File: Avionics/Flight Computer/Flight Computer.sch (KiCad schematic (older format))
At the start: 28 parts, among them U10 Logo, U11 Logo, U6 LP5521YQ

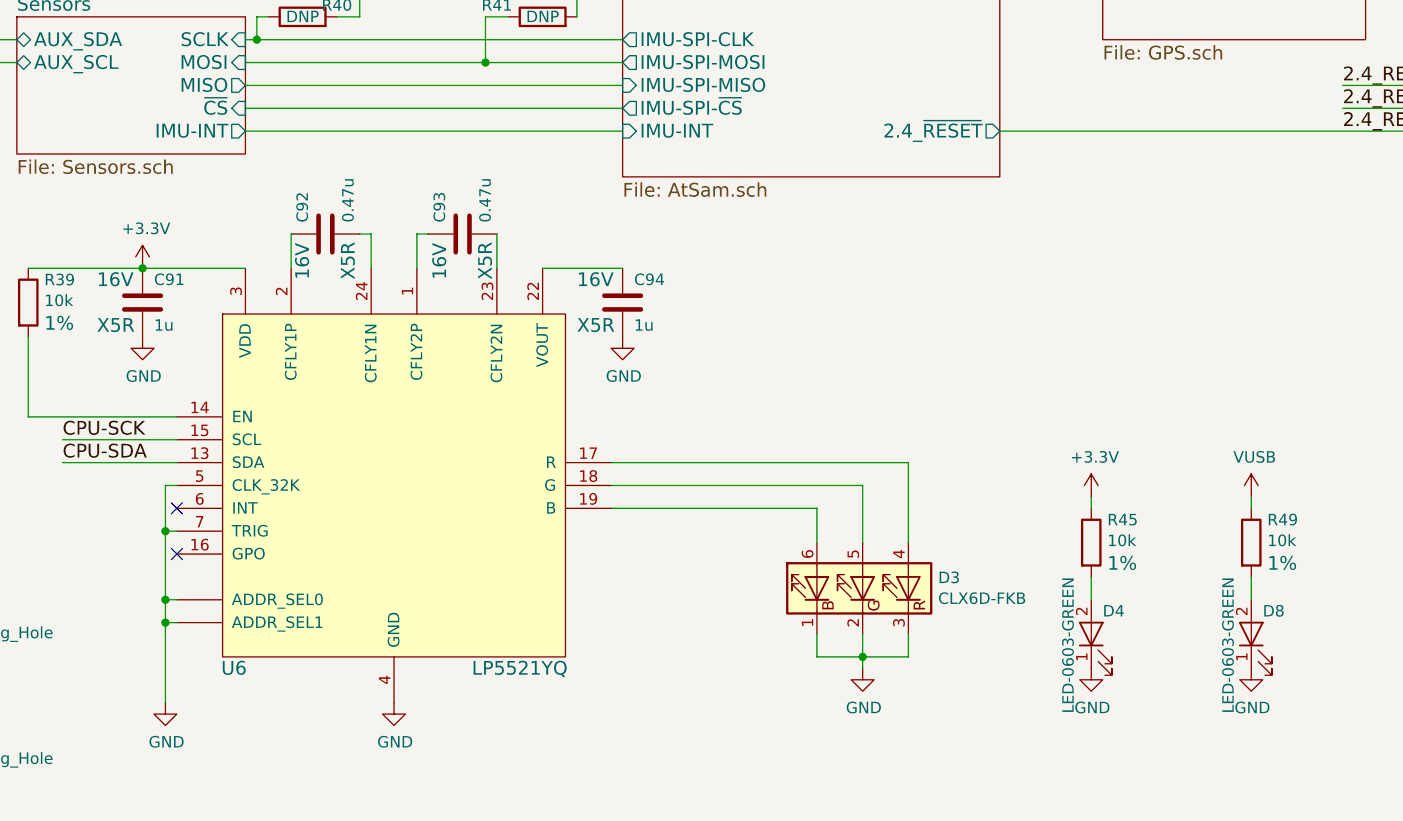
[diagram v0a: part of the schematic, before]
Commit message: Updated more manufacturing part numbers for macrofab compatibility.
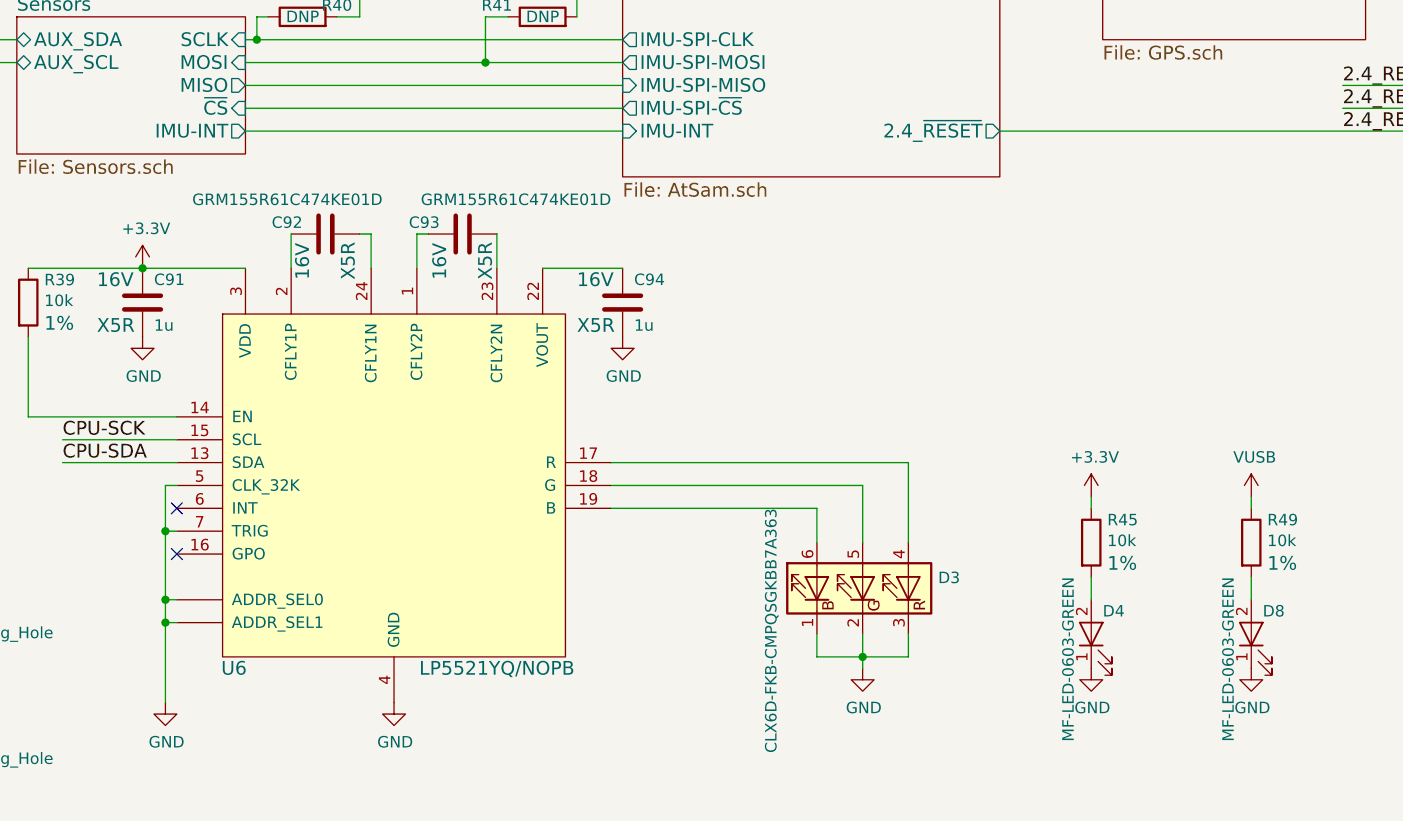
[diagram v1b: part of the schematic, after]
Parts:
- C92, C93: value 0.47u -> GRM155R61C474KE01D
- D3: value CLX6D-FKB -> CLX6D-FKB-CMPQSGKBB7A363
- D4, D8: value LED-0603-GREEN -> MF-LED-0603-GREEN
- U6: value LP5521YQ -> LP5521YQ/NOPB
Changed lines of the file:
@@
 P 5850 7100
 F 0 "D4" V 5950 7050 50  0000 R CNN
-F 1 "LED-0603-GREEN" H 6100 7200 50  0000 R CNN
+F 1 "MF-LED-0603-GREEN" H 6100 7200 50  0000 R CNN
 F 2 "LEDs:LED_0603" H 450 750 50  0001 C CNN
 F 3 "https://s3.amazonaws.com/mfprodpublic/datasheets/S_110_LTST-C190KGKT.pdf" H 450 750 50  0001 C CNN
@@
 P 6550 7100
 F 0 "D8" V 6650 7050 50  0000 R CNN
-F 1 "LED-0603-GREEN" H 6800 7200 50  0000 R CNN
+F 1 "MF-LED-0603-GREEN" H 6800 7200 50  0000 R CNN
 F 2 "LEDs:LED_0603" H 1150 750 50  0001 C CNN
 F 3 "https://s3.amazonaws.com/mfprodpublic/datasheets/S_110_LTST-C190KGKT.pdf" H 1150 750 50  0001 C CNN
@@
 P 4850 6900
 F 0 "D3" V 4896 6570 50  0000 R CNN
-F 1 "CLX6D-FKB" V 4805 6570 50  0000 R CNN
+F 1 "CLX6D-FKB-CMPQSGKBB7A363" H 5200 7300 50  0000 R CNN
 F 2 "LEDs:LED_PLCC6_3.4x3.4mm" H 200 150 50  0001 C CNN
 F 3 "http://www.cree.com/~/media/Files/Cree/LED-Components-and-Modules/HB/Data-Sheets/1278-CLX6D-FKB.pdf" H 200 150 50  0001 C CNN
@@
 U 1 1 58CBE629
 P 2500 5350
-F 0 "C92" H 2550 5450 50  0000 L CNN
-F 1 "0.47u" H 2550 5250 50  0000 L CNN
+F 0 "C92" V 2550 5450 50  0000 L CNN
+F 1 "GRM155R61C474KE01D" V 2650 5100 50  0000 L CNN
 F 2 "Capacitors_SMD:C_0402" H -4012 4050 50  0001 C CNN
 F 3 "" H -4050 4200 50  0001 C CNN
@@
 U 1 1 58CBEC69
 P 3100 5350
-F 0 "C93" H 3150 5450 50  0000 L CNN
-F 1 "0.47u" H 3150 5250 50  0000 L CNN
+F 0 "C93" V 3150 5450 50  0000 L CNN
+F 1 "GRM155R61C474KE01D" V 3250 4700 50  0000 L CNN
 F 2 "Capacitors_SMD:C_0402" H -3412 4050 50  0001 C CNN
 F 3 "" H -3450 4200 50  0001 C CNN
@@
 P 2800 6450
 F 0 "U6" H 2100 5650 60  0000 C CNN
-F 1 "LP5521YQ" H 3350 5650 60  0000 C CNN
+F 1 "LP5521YQ/NOPB" H 3250 5650 60  0000 C CNN
 F 2 "Housings_DFN_QFN:QFN-24-1EP_4x5mm_Pitch0.5mm" H -150 -800 60  0001 C CNN
 F 3 "http://www.digikey.com/product-detail/en/texas-instruments/LP5521YQ-NOPB/LP5521YQ-NOPBCT-ND/1836170" H -200 -950 60  0001 C CNN

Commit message: Finished rerouting and power supply update. Replaced connectors and did initial replacement.
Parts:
- added MK3, MK4: Mounting_Hole, Mounting_Holes:MountingHole_2.5mm, symbol Mounting_Hole
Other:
- moved on the sheet: MK1, MK2
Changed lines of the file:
@@
 LIBS:Power_Management
 LIBS:powerint
+LIBS:onsemi
 LIBS:Flight Computer-cache
 EELAYER 26 0
@@
 L Mounting_Hole MK1
 U 1 1 58BDD655
-P 700 7050
-F 0 "MK1" H 800 7096 50  0000 L CNN
-F 1 "Mounting_Hole" H 800 7005 50  0000 L CNN
-F 2 "Mounting_Holes:MountingHole_2.5mm" H -3500 0   50  0001 C CNN
-F 3 "" H -3500 0   50  0001 C CNN
-	1    700  7050
+P 700 6550
+F 0 "MK1" H 800 6596 50  0000 L CNN
+F 1 "Mounting_Hole" H 800 6505 50  0000 L CNN
+F 2 "Mounting_Holes:MountingHole_2.5mm" H -3500 -500 50  0001 C CNN
+F 3 "" H -3500 -500 50  0001 C CNN
+	1    700  6550
 	1    0    0    -1
 $EndComp
@@
 L Mounting_Hole MK2
 U 1 1 58BDE299
-P 700 7600
-F 0 "MK2" H 800 7646 50  0000 L CNN
-F 1 "Mounting_Hole" H 800 7555 50  0000 L CNN
-F 2 "Mounting_Holes:MountingHole_2.5mm" H -3500 550 50  0001 C CNN
-F 3 "" H -3500 550 50  0001 C CNN
-	1    700  7600
+P 700 6850
+F 0 "MK2" H 800 6896 50  0000 L CNN
+F 1 "Mounting_Hole" H 800 6805 50  0000 L CNN
+F 2 "Mounting_Holes:MountingHole_2.5mm" H -3500 -200 50  0001 C CNN
+F 3 "" H -3500 -200 50  0001 C CNN
+	1    700  6850
 	1    0    0    -1
 $EndComp
@@
 	1    0    0    -1
 $EndComp
+$Comp
+L Mounting_Hole MK3
+U 1 1 58E001FE
+P 700 7150
+F 0 "MK3" H 800 7196 50  0000 L CNN
+F 1 "Mounting_Hole" H 800 7105 50  0000 L CNN
+F 2 "Mounting_Holes:MountingHole_2.5mm" H -3500 100 50  0001 C CNN
+F 3 "" H -3500 100 50  0001 C CNN
+	1    700  7150
+	1    0    0    -1
+$EndComp
+$Comp
+L Mounting_Hole MK4
+U 1 1 58E00204
+P 700 7450
+F 0 "MK4" H 800 7496 50  0000 L CNN
+F 1 "Mounting_Hole" H 800 7405 50  0000 L CNN
+F 2 "Mounting_Holes:MountingHole_2.5mm" H -3500 400 50  0001 C CNN
+F 3 "" H -3500 400 50  0001 C CNN
+	1    700  7450
+	1    0    0    -1
+$EndComp
